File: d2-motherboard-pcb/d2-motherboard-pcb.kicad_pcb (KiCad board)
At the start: 4 copper layers, 61.8 x 40 mm, 59 parts, among them J2 Conn_01x02_Male, J4 Conn_01x04_Male, M1 Screw_Terminal_01x02, M2 Screw_Terminal_01x02, M3 Screw_Terminal_01x02, M4 Screw_Terminal_01x02, U1 PIC32CM6408MC00032-I/PT, U2 L9958, U3 L9958, U4 L9958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

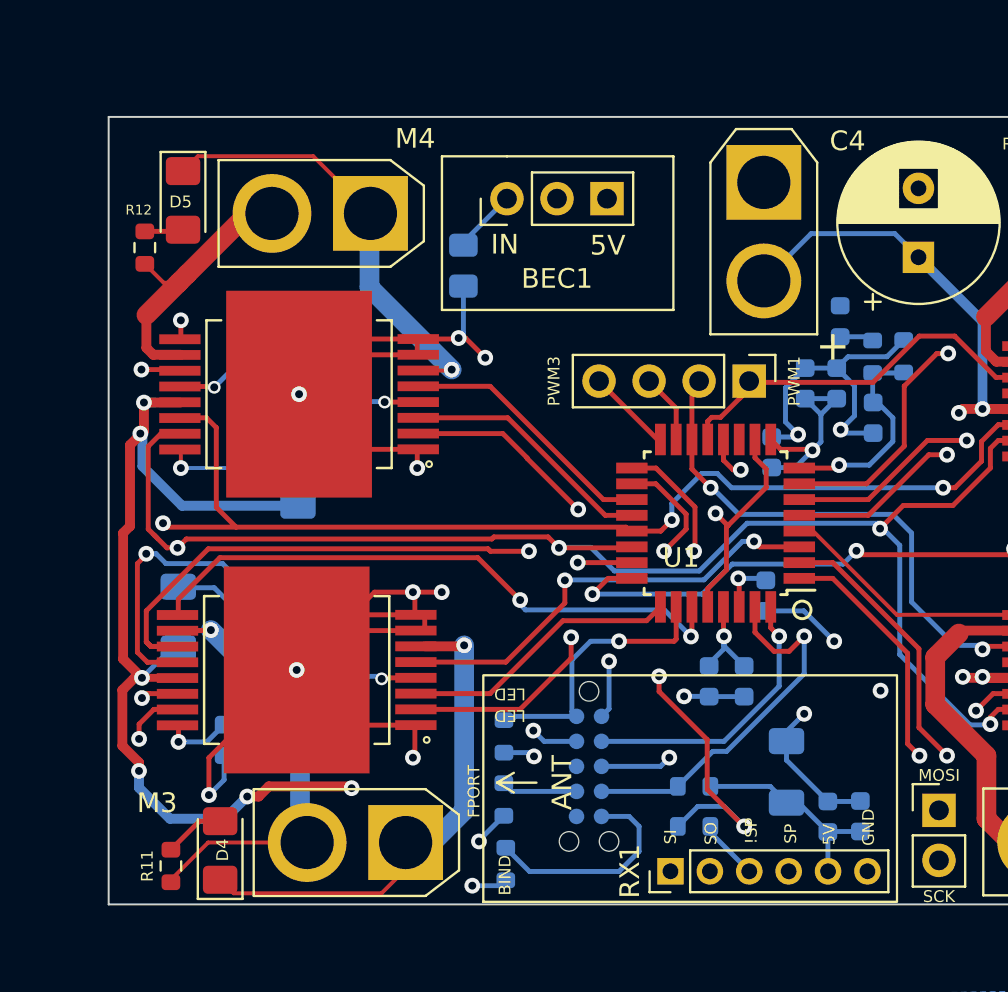
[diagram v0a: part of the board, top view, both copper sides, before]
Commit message: add debug board
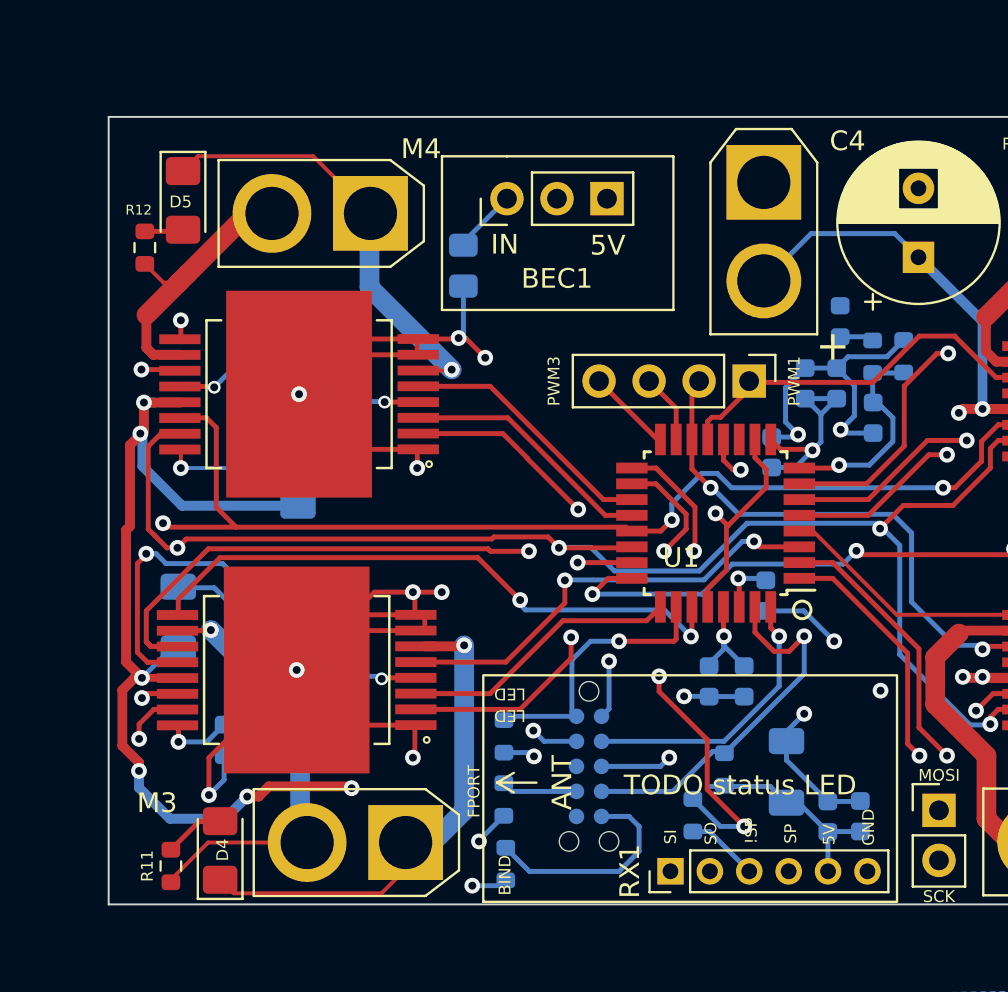
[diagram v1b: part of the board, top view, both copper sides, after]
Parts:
- moved R8 1.76 mm to (138.7, 85.5), turned to 90 degrees
- moved R14 0.57 mm to (137.1, 87.8), turned to -90 degrees
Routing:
- net RX_FPORT_RX_SERCOM0: track 27.9 -> 26.9 mm
- net Net-(R14-Pad2): track 2.79 -> 3.70 mm
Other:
- board text added: "TODO status LED"
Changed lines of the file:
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@@
     (property "Sheetname" "Channel4")
     (attr through_hole)
-    (fp_text reference "M4" (at -2.269 3.8 180) (layer "F.SilkS")
+    (fp_text reference "M4" (at -2.569 3.275 180) (layer "F.SilkS")
       (effects (font (size 1 1) (thickness 0.15)))
     )
@@
   )
   (footprint "Resistor_SMD:R_0603_1608Metric" (layer "B.Cu")
-    (at 137.16 86.36 180)
+    (at 138.7 85.5 90)
     (descr "Resistor SMD 0603 (1608 Metric), square (rectangular) end terminal, IPC_7351 nominal, (Body size source: IPC-SM-782 page 72, https://www.pcb-3d.com/wordpress/wp-content/uploads/ipc-sm-782a_amendment_1_and_2.pdf), generated with kicad-footprint-generator")
     (tags "resistor")
@@
     (property "Sheetname" "")
     (attr smd)
-    (fp_text reference "R8" (at 0.04 1.32) (layer "B.SilkS")
+    (fp_text reference "R8" (at -0.1 -1.4 90) (layer "B.SilkS")
       (effects (font (size 0.6 0.6) (thickness 0.15)) (justify mirror))
     )
-    (fp_text value "1k 1%" (at 0 -1.43) (layer "B.Fab")
-      (effects (font (size 1 1) (thickness 0.15)) (justify mirror))
-    )
-    (fp_text user "${REFERENCE}" (at 0 0) (layer "B.Fab")
+    (fp_text value "1k 1%" (at 0 -1.43 90) (layer "B.Fab")
+      (effects (font (size 1 1) (thickness 0.15)) (justify mirror))
+    )
+    (fp_text user "${REFERENCE}" (at 0 0 90) (layer "B.Fab")
       (effects (font (size 0.4 0.4) (thickness 0.06)) (justify mirror))
     )
@@
     (fp_line (start -0.8 0.4125) (end 0.8 0.4125) (layer "B.Fab") (width 0.1))
     (fp_line (start 0.8 -0.4125) (end -0.8 -0.4125) (layer "B.Fab") (width 0.1))
-    (pad "1" smd roundrect (at -0.825 0 180) (size 0.8 0.95) (layers "B.Cu" "B.Paste" "B.Mask") (roundrect_rratio 0.25)
+    (pad "1" smd roundrect (at -0.825 0 90) (size 0.8 0.95) (layers "B.Cu" "B.Paste" "B.Mask") (roundrect_rratio 0.25)
       (net 1 "5V") (pintype "passive"))
-    (pad "2" smd roundrect (at 0.825 0 180) (size 0.8 0.95) (layers "B.Cu" "B.Paste" "B.Mask") (roundrect_rratio 0.25)
+    (pad "2" smd roundrect (at 0.825 0 90) (size 0.8 0.95) (layers "B.Cu" "B.Paste" "B.Mask") (roundrect_rratio 0.25)
       (net 36 "SWCLK") (pintype "passive"))
     (model "${KICAD6_3DMODEL_DIR}/Resistor_SMD.3dshapes/R_0603_1608Metric.wrl"
@@
   )
   (footprint "Resistor_SMD:R_0603_1608Metric" (layer "B.Cu")
-    (at 137.16 88.392)
+    (at 137.1 87.825 -90)
     (descr "Resistor SMD 0603 (1608 Metric), square (rectangular) end terminal, IPC_7351 nominal, (Body size source: IPC-SM-782 page 72, https://www.pcb-3d.com/wordpress/wp-content/uploads/ipc-sm-782a_amendment_1_and_2.pdf), generated with kicad-footprint-generator")
     (tags "resistor")
@@
     (property "Sheetname" "")
     (attr smd)
-    (fp_text reference "R14" (at 0 -1.016) (layer "B.SilkS")
+    (fp_text reference "R14" (at 0 -1.016 90) (layer "B.SilkS")
       (effects (font (size 0.5 0.5) (thickness 0.125)) (justify mirror))
     )
-    (fp_text value "?k 1%" (at 0 -1.43) (layer "B.Fab")
-      (effects (font (size 1 1) (thickness 0.15)) (justify mirror))
-    )
-    (fp_text user "${REFERENCE}" (at 0 0) (layer "B.Fab")
+    (fp_text value "?k 1%" (at 0 -1.43 90) (layer "B.Fab")
+      (effects (font (size 1 1) (thickness 0.15)) (justify mirror))
+    )
+    (fp_text user "${REFERENCE}" (at 0 0 90) (layer "B.Fab")
       (effects (font (size 0.4 0.4) (thickness 0.06)) (justify mirror))
     )
@@
     (fp_line (start -0.8 0.4125) (end 0.8 0.4125) (layer "B.Fab") (width 0.1))
     (fp_line (start 0.8 -0.4125) (end -0.8 -0.4125) (layer "B.Fab") (width 0.1))
-    (pad "1" smd roundrect (at -0.825 0) (size 0.8 0.95) (layers "B.Cu" "B.Paste" "B.Mask") (roundrect_rratio 0.25)
+    (pad "1" smd roundrect (at -0.825 0 270) (size 0.8 0.95) (layers "B.Cu" "B.Paste" "B.Mask") (roundrect_rratio 0.25)
       (net 8 "RX_FPORT_RX_SERCOM0") (pintype "passive"))
-    (pad "2" smd roundrect (at 0.825 0) (size 0.8 0.95) (layers "B.Cu" "B.Paste" "B.Mask") (roundrect_rratio 0.25)
+    (pad "2" smd roundrect (at 0.825 0 270) (size 0.8 0.95) (layers "B.Cu" "B.Paste" "B.Mask") (roundrect_rratio 0.25)
       (net 49 "Net-(R14-Pad2)") (pintype "passive"))
     (model "${KICAD6_3DMODEL_DIR}/Resistor_SMD.3dshapes/R_0603_1608Metric.wrl"
@@
   (gr_text "FPORT" (at 125.984 86.614 90) (layer "F.SilkS")
     (effects (font (size 0.6 0.6) (thickness 0.15)))
+  )
+  (gr_text "TODO status LED" (at 139.5 86.3) (layer "F.SilkS")
+    (effects (font (size 1 1) (thickness 0.15)))
   )
   (gr_text "hmm idk bout this placement\nmaybe make the RX RA\nand then for {dblquote}debug{dblquote} units, put connectors there\nfor prod, leave them unpopulated and mount it vert" (at 137.922 93.98) (layer "Cmts.User")
@@
   (segment (start 114.475 86.875) (end 115.055 86.875) (width 0.5) (layer "F.Cu") (net 2))
   (segment (start 153.9 67.2) (end 151.8 67.2) (width 0.5) (layer "F.Cu") (net 2))
+  (segment (start 108.525 69.031) (end 108.525 73.15) (width 0.5) (layer "F.Cu") (net 2))
   (segment (start 109.131 80.85) (end 108.755767 80.85) (width 0.5) (layer "F.Cu") (net 2))
   (segment (start 115.57 86.36) (end 119.685 86.36) (width 0.5) (layer "F.Cu") (net 2))
-  (segment (start 109.156 68.4) (end 108.525 69.031) (width 0.5) (layer "F.Cu") (net 2))
   (segment (start 109.231 66.875) (end 111.081 66.875) (width 0.5) (layer "F.Cu") (net 2))
+  (segment (start 109.231 68.325) (end 108.525 69.031) (width 0.5) (layer "F.Cu") (net 2))
   (segment (start 151.8 80.8) (end 151.6 80.8) (width 0.5) (layer "F.Cu") (net 2))
   (segment (start 150.8 80.8) (end 151.8 80.8) (width 0.25) (layer "F.Cu") (net 2))
   (segment (start 108.755767 80.85) (end 108.136 81.469767) (width 0.5) (layer "F.Cu") (net 2))
   (segment (start 119.685 86.36) (end 119.775 86.45) (width 0.5) (layer "F.Cu") (net 2))
+  (segment (start 108.525 73.15) (end 108.325 73.35) (width 0.5) (layer "F.Cu") (net 2))
   (segment (start 115.055 86.875) (end 115.57 86.36) (width 0.5) (layer "F.Cu") (net 2))
+  (segment (start 109.231 66.875) (end 109.231 68.325) (width 0.5) (layer "F.Cu") (net 2))
   (segment (start 153.9 80.85) (end 151.85 80.85) (width 0.5) (layer "F.Cu") (net 2))
   (segment (start 108.981 85.147082) (end 108.981 85.575) (width 0.5) (layer "F.Cu") (net 2))
   (segment (start 109.131 80.85) (end 108.781 80.85) (width 0.5) (layer "F.Cu") (net 2))
   (segment (start 150.85 80.85) (end 150.8 80.8) (width 0.5) (layer "F.Cu") (net 2))
-  (segment (start 108.525 69.031) (end 108.525 73.15) (width 0.5) (layer "F.Cu") (net 2))
   (segment (start 151.8 67.2) (end 150.8 67.2) (width 0.5) (layer "F.Cu") (net 2))
-  (segment (start 108.175 79.894) (end 109.131 80.85) (width 0.5) (layer "F.Cu") (net 2))
-  (segment (start 109.231 66.875) (end 109.231 68.325) (width 0.5) (layer "F.Cu") (net 2))
-  (segment (start 108.525 73.15) (end 108.175 73.5) (width 0.5) (layer "F.Cu") (net 2))
+  (segment (start 108.325 80.044) (end 109.131 80.85) (width 0.5) (layer "F.Cu") (net 2))
   (segment (start 109.131 80.85) (end 110.926 80.85) (width 0.4) (layer "F.Cu") (net 2))
-  (segment (start 108.175 73.5) (end 108.175 79.894) (width 0.5) (layer "F.Cu") (net 2))
+  (segment (start 108.325 73.35) (end 108.325 80.044) (width 0.5) (layer "F.Cu") (net 2))
   (segment (start 151.85 80.85) (end 151.8 80.8) (width 0.5) (layer "F.Cu") (net 2))
   (segment (start 108.136 84.302082) (end 108.981 85.147082) (width 0.5) (layer "F.Cu") (net 2))
   (segment (start 108.136 81.469767) (end 108.136 84.302082) (width 0.5) (layer "F.Cu") (net 2))
-  (segment (start 109.231 68.325) (end 109.156 68.4) (width 0.5) (layer "F.Cu") (net 2))
   (segment (start 150.8 67.2) (end 150.6 67.4) (width 0.5) (layer "F.Cu") (net 2))
   (via (at 114.475 86.875) (size 0.8) (drill 0.4) (layers "F.Cu" "B.Cu") (net 2))
@@
   (segment (start 135.6 80.554) (end 135.382 80.772) (width 0.25) (layer "In1.Cu") (net 8))
   (segment (start 139.524952 72.311048) (end 139.524952 70.295048) (width 0.25) (layer "In1.Cu") (net 8))
-  (segment (start 136.335 88.392) (end 137.351 87.376) (width 0.25) (layer "B.Cu") (net 8))
-  (segment (start 137.351 87.376) (end 138.684 87.376) (width 0.25) (layer "B.Cu") (net 8))
-  (segment (start 138.684 87.376) (end 139.7 88.392) (width 0.25) (layer "B.Cu") (net 8))
+  (segment (start 138.492 88.392) (end 139.7 88.392) (width 0.25) (layer "B.Cu") (net 8))
+  (segment (start 137.1 87) (end 138.492 88.392) (width 0.25) (layer "B.Cu") (net 8))
   (segment (start 126.18 74.75) (end 128.33 76.9) (width 0.25) (layer "F.Cu") (net 9))
   (segment (start 113.086 74.75) (end 126.18 74.75) (width 0.25) (layer "F.Cu") (net 9))
@@
   (segment (start 127.5 86.2) (end 127.914 86.614) (width 0.25) (layer "B.Cu") (net 48))
   (segment (start 127.914 86.614) (end 131.191 86.614) (width 0.25) (layer "B.Cu") (net 48))
-  (segment (start 137.985 88.695) (end 139.96 90.67) (width 0.25) (layer "B.Cu") (net 49))
+  (segment (start 137.94 88.65) (end 139.96 90.67) (width 0.25) (layer "B.Cu") (net 49))
+  (segment (start 137.1 88.65) (end 137.94 88.65) (width 0.25) (layer "B.Cu") (net 49))
   (segment (start 165.95 67.2) (end 164.2 67.2) (width 0.25) (layer "F.Cu") (net 50))
   (via (at 164.2 67.2) (size 0.65) (drill 0.4) (layers "F.Cu" "B.Cu") (net 50))

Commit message: rev2
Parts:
- removed SWD3: Connector:Tag-Connect_TC2050-IDC-NL_2x05_P1.27mm_Vertical, Connector:Tag-Connect_TC2050-IDC-NL_2x05_P1.27mm_Vertical
- added C25: 1uF, Capacitor_SMD:C_0603_1608Metric, B.Cu at (143.3, 76.7)
- added D2: LED, LED_SMD:LED_0603_1608Metric_Pad1.05x0.95mm_HandSolder, F.Cu at (129.3, 66.3)
- added R16: 330, Resistor_SMD:R_0603_1608Metric, F.Cu at (127.8, 64.0)
- added SWD1: Connector:Tag-Connect_TC2050-IDC-NL_2x05_P1.27mm_Vertical, Connector:Tag-Connect_TC2050-IDC-NL_2x05_P1.27mm_Vertical, B.Cu at (131.8, 85.3)
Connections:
- U1 pad 11: RX_FPORT_TX -> RX_FPORT_RX_SERCOM0
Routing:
- net GND: track 180.7 -> 196.4 mm
- net FTDI_RXI: track 29.2 -> 35.1 mm
- net 5V: track 46.8 -> 51.1 mm, vias 8 -> 9
- net Net-(D2-Pad1): track 0.00 -> 1.77 mm
- net EN1: track 17.6 -> 16.1 mm
- net PWM1: track 20.9 -> 19.6 mm
- net RX_FPORT_RX_SERCOM0: track 26.9 -> 27.7 mm
- net RESET: track 13.8 -> 13.3 mm
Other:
- board text removed: "PWM3"
- board text removed: "TODO status LED"
- board text removed: "hmm idk bout this placement maybe make the RX RA and then for {dblquote}debug{dblquote} units, put connectors there for prod, leave them unpopulated and mount it vert"
